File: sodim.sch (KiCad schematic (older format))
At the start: 1 part, among them J1 ddr4-sodimm-edge-connector

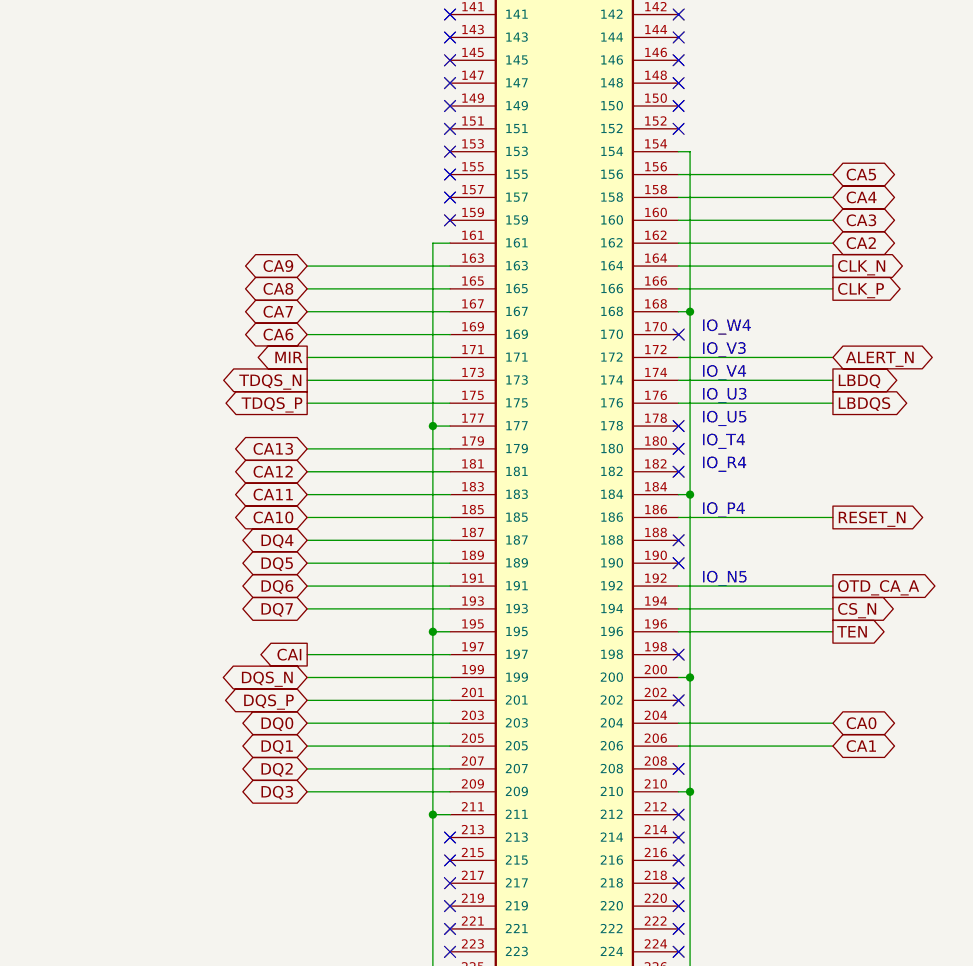
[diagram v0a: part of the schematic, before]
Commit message: Update pin assignment
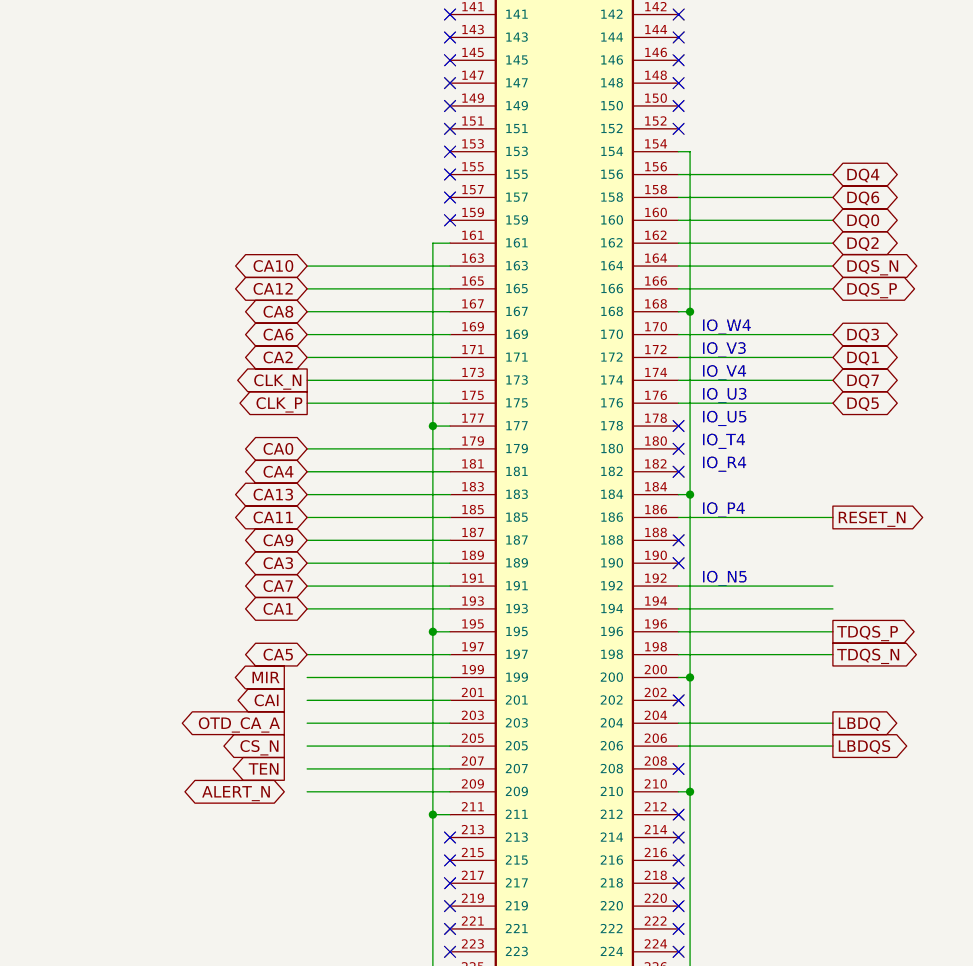
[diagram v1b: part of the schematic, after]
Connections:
- wire segments 183 -> 185
- no-connect marks 149 -> 147
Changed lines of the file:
@@
 Connection ~ 10550 5200
 Wire Wire Line
-	10550 5200 10550 6000
-Wire Wire Line
 	10500 5600 11175 5600
 Wire Wire Line
@@
 Wire Wire Line
 	4075 8900 4725 8900
-Text GLabel 8875 5400 0    50   BiDi ~ 0
+Text GLabel 11175 3800 2    50   BiDi ~ 0
 DQ4
-Text GLabel 8875 5500 0    50   BiDi ~ 0
+Text GLabel 11175 4800 2    50   BiDi ~ 0
 DQ5
-Text GLabel 8875 5600 0    50   BiDi ~ 0
+Text GLabel 11175 3900 2    50   BiDi ~ 0
 DQ6
-Text GLabel 8875 5700 0    50   BiDi ~ 0
+Text GLabel 11175 4700 2    50   BiDi ~ 0
 DQ7
-Text GLabel 8875 6500 0    50   BiDi ~ 0
+Text GLabel 11175 4500 2    50   BiDi ~ 0
 DQ3
-Text GLabel 8875 6400 0    50   BiDi ~ 0
+Text GLabel 11175 4100 2    50   BiDi ~ 0
 DQ2
-Text GLabel 8875 6300 0    50   BiDi ~ 0
+Text GLabel 11175 4600 2    50   BiDi ~ 0
 DQ1
-Text GLabel 8875 6200 0    50   BiDi ~ 0
+Text GLabel 11175 4000 2    50   BiDi ~ 0
 DQ0
-Text GLabel 11175 4300 2    50   Output ~ 0
-CLK_P
-Text GLabel 11175 4200 2    50   Output ~ 0
-CLK_N
-Text GLabel 11175 6200 2    50   BiDi ~ 0
-CA0
-Text GLabel 11175 5700 2    50   Output ~ 0
-CS_N
 Text GLabel 11175 5300 2    50   Output ~ 0
 RESET_N
-Text GLabel 11175 5600 2    50   Output ~ 0
+Text GLabel 8775 6200 0    50   Output ~ 0
 OTD_CA_A
-Text GLabel 8875 4800 0    50   Output ~ 0
-TDQS_P
-Text GLabel 8875 4700 0    50   Output ~ 0
-TDQS_N
-Text GLabel 8875 6100 0    50   BiDi ~ 0
-DQS_P
-Text GLabel 8875 6000 0    50   BiDi ~ 0
-DQS_N
-Text GLabel 11175 6300 2    50   BiDi ~ 0
-CA1
-Text GLabel 11175 4100 2    50   BiDi ~ 0
-CA2
-Text GLabel 11175 4000 2    50   BiDi ~ 0
-CA3
-Text GLabel 11175 3900 2    50   BiDi ~ 0
-CA4
-Text GLabel 11175 3800 2    50   BiDi ~ 0
-CA5
-Text GLabel 8875 4500 0    50   BiDi ~ 0
-CA6
-Text GLabel 8875 4400 0    50   BiDi ~ 0
-CA7
-Text GLabel 8875 4300 0    50   BiDi ~ 0
-CA8
-Text GLabel 8875 4200 0    50   BiDi ~ 0
-CA9
-Text GLabel 8875 5300 0    50   BiDi ~ 0
-CA10
-Text GLabel 8875 5200 0    50   BiDi ~ 0
-CA11
-Text GLabel 8875 5100 0    50   BiDi ~ 0
-CA12
-Text GLabel 8875 5000 0    50   BiDi ~ 0
-CA13
-Text GLabel 11175 4700 2    50   Output ~ 0
+Text GLabel 11175 6200 2    50   Output ~ 0
 LBDQ
-Text GLabel 11175 4800 2    50   Output ~ 0
+Text GLabel 11175 6300 2    50   Output ~ 0
 LBDQS
-Text GLabel 11175 5800 2    50   Output ~ 0
+Text GLabel 8775 6400 0    50   Output ~ 0
 TEN
-Text GLabel 8875 4600 0    50   Output ~ 0
-MIR
-Text GLabel 8875 5900 0    50   Output ~ 0
+Text GLabel 8775 6100 0    50   Output ~ 0
 CAI
 Wire Wire Line
 	10500 4600 11175 4600
-Text GLabel 11175 4600 2    50   BiDi ~ 0
+Text GLabel 8775 6500 0    50   BiDi ~ 0
 ALERT_N
-NoConn ~ 10500 4500
 NoConn ~ 10500 4900
 NoConn ~ 10500 5000
@@
 NoConn ~ 10500 7100
 NoConn ~ 10500 6400
-NoConn ~ 10500 5900
 NoConn ~ 9500 3700
 NoConn ~ 9500 3800
@@
 NoConn ~ 10500 8400
 NoConn ~ 10500 8500
+Text GLabel 8775 6300 0    50   Output ~ 0
+CS_N
+Text GLabel 8875 5200 0    50   BiDi ~ 0
+CA13
+Text GLabel 8875 4300 0    50   BiDi ~ 0
+CA12
+Text GLabel 8875 5300 0    50   BiDi ~ 0
+CA11
+Text GLabel 8875 4200 0    50   BiDi ~ 0
+CA10
+Text GLabel 8875 5700 0    50   BiDi ~ 0
+CA1
+Text GLabel 8875 5000 0    50   BiDi ~ 0
+CA0
+Text GLabel 8875 5400 0    50   BiDi ~ 0
+CA9
+Text GLabel 8875 4400 0    50   BiDi ~ 0
+CA8
+Text GLabel 8875 5600 0    50   BiDi ~ 0
+CA7
+Text GLabel 8875 4500 0    50   BiDi ~ 0
+CA6
+Text GLabel 8775 6000 0    50   Output ~ 0
+MIR
+Text GLabel 8875 5900 0    50   BiDi ~ 0
+CA5
+Text GLabel 8875 5100 0    50   BiDi ~ 0
+CA4
+Text GLabel 8875 5500 0    50   BiDi ~ 0
+CA3
+Text GLabel 8875 4600 0    50   BiDi ~ 0
+CA2
+Text GLabel 11175 4200 2    50   BiDi ~ 0
+DQS_N
+Text GLabel 11175 4300 2    50   BiDi ~ 0
+DQS_P
+Text GLabel 8875 4700 0    50   Output ~ 0
+CLK_N
+Text GLabel 8875 4800 0    50   Output ~ 0
+CLK_P
+Text GLabel 11175 5900 2    50   Output ~ 0
+TDQS_N
+Text GLabel 11175 5800 2    50   Output ~ 0
+TDQS_P
+Wire Wire Line
+	10550 5200 10550 6000
+Wire Wire Line
+	10500 5900 11175 5900
+Wire Wire Line
+	10500 4500 11175 4500
 $EndSCHEMATC

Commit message: Update signal assignment
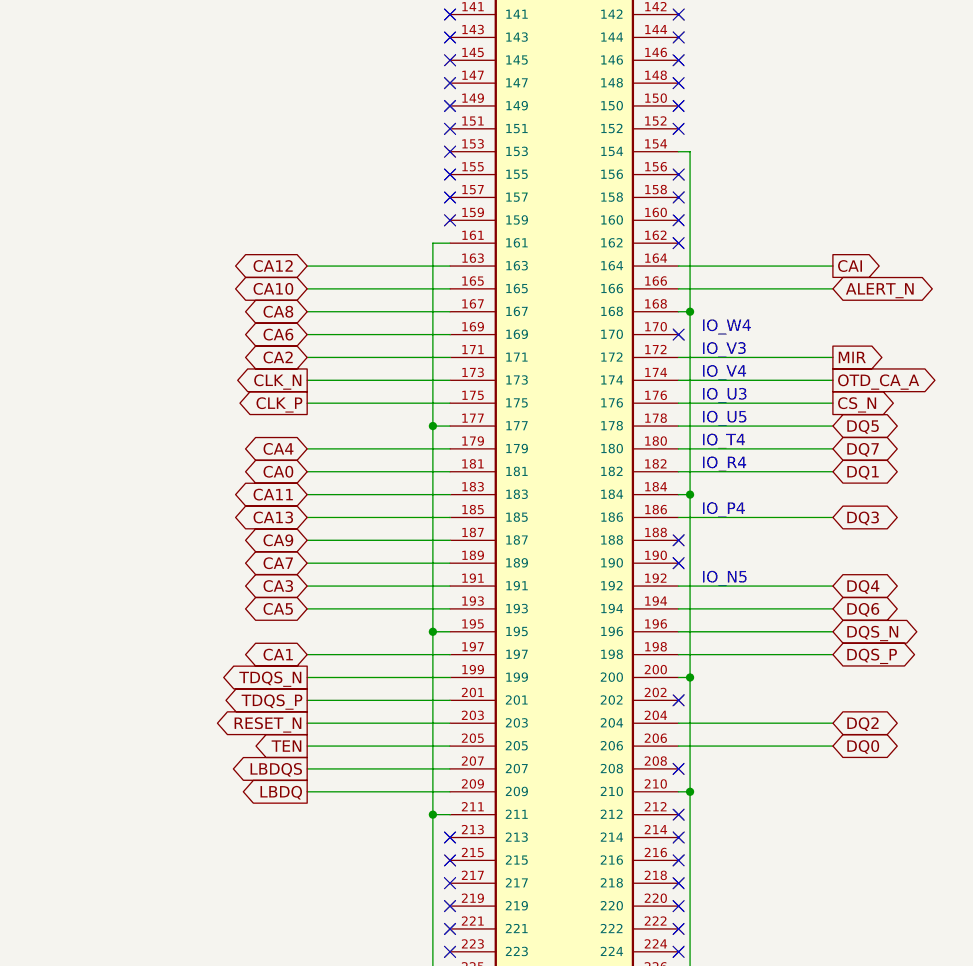
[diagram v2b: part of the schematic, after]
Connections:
- wire segments 185 -> 183
- no-connect marks 147 -> 149
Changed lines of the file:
@@
 $EndComp
 Wire Wire Line
-	10500 3800 11175 3800
-Wire Wire Line
-	10500 3900 11175 3900
-Wire Wire Line
-	10500 4000 11175 4000
-Wire Wire Line
-	10500 4100 11175 4100
-Wire Wire Line
 	10500 4200 11175 4200
 Wire Wire Line
@@
 Wire Wire Line
 	4075 8900 4725 8900
-Text GLabel 11175 3800 2    50   BiDi ~ 0
+Text GLabel 11175 5600 2    50   BiDi ~ 0
 DQ4
-Text GLabel 11175 4800 2    50   BiDi ~ 0
+Text GLabel 11175 4900 2    50   BiDi ~ 0
 DQ5
-Text GLabel 11175 3900 2    50   BiDi ~ 0
+Text GLabel 11175 5700 2    50   BiDi ~ 0
 DQ6
-Text GLabel 11175 4700 2    50   BiDi ~ 0
+Text GLabel 11175 5000 2    50   BiDi ~ 0
 DQ7
-Text GLabel 11175 4500 2    50   BiDi ~ 0
+Text GLabel 11175 5300 2    50   BiDi ~ 0
 DQ3
-Text GLabel 11175 4100 2    50   BiDi ~ 0
+Text GLabel 11175 6200 2    50   BiDi ~ 0
 DQ2
-Text GLabel 11175 4600 2    50   BiDi ~ 0
+Text GLabel 11175 5100 2    50   BiDi ~ 0
 DQ1
-Text GLabel 11175 4000 2    50   BiDi ~ 0
+Text GLabel 11175 6300 2    50   BiDi ~ 0
 DQ0
-Text GLabel 11175 5300 2    50   Output ~ 0
+Text GLabel 8875 6200 0    50   Output ~ 0
 RESET_N
-Text GLabel 8775 6200 0    50   Output ~ 0
+Text GLabel 11175 4700 2    50   Output ~ 0
 OTD_CA_A
-Text GLabel 11175 6200 2    50   Output ~ 0
+Text GLabel 8875 6500 0    50   Output ~ 0
 LBDQ
-Text GLabel 11175 6300 2    50   Output ~ 0
+Text GLabel 8875 6400 0    50   Output ~ 0
 LBDQS
-Text GLabel 8775 6400 0    50   Output ~ 0
+Text GLabel 8875 6300 0    50   Output ~ 0
 TEN
-Text GLabel 8775 6100 0    50   Output ~ 0
+Text GLabel 11175 4200 2    50   Output ~ 0
 CAI
 Wire Wire Line
 	10500 4600 11175 4600
-Text GLabel 8775 6500 0    50   BiDi ~ 0
+Text GLabel 11175 4300 2    50   BiDi ~ 0
 ALERT_N
-NoConn ~ 10500 4900
-NoConn ~ 10500 5000
-NoConn ~ 10500 5100
 Wire Wire Line
 	10500 4700 11175 4700
@@
 NoConn ~ 10500 8400
 NoConn ~ 10500 8500
-Text GLabel 8775 6300 0    50   Output ~ 0
+Text GLabel 11175 4800 2    50   Output ~ 0
 CS_N
-Text GLabel 8875 5200 0    50   BiDi ~ 0
+Text GLabel 8875 5300 0    50   BiDi ~ 0
 CA13
-Text GLabel 8875 4300 0    50   BiDi ~ 0
+Text GLabel 8875 4200 0    50   BiDi ~ 0
 CA12
-Text GLabel 8875 5300 0    50   BiDi ~ 0
+Text GLabel 8875 5200 0    50   BiDi ~ 0
 CA11
-Text GLabel 8875 4200 0    50   BiDi ~ 0
+Text GLabel 8875 4300 0    50   BiDi ~ 0
 CA10
-Text GLabel 8875 5700 0    50   BiDi ~ 0
+Text GLabel 8875 5900 0    50   BiDi ~ 0
 CA1
-Text GLabel 8875 5000 0    50   BiDi ~ 0
+Text GLabel 8875 5100 0    50   BiDi ~ 0
 CA0
 Text GLabel 8875 5400 0    50   BiDi ~ 0
@@
 Text GLabel 8875 4400 0    50   BiDi ~ 0
 CA8
-Text GLabel 8875 5600 0    50   BiDi ~ 0
+Text GLabel 8875 5500 0    50   BiDi ~ 0
 CA7
 Text GLabel 8875 4500 0    50   BiDi ~ 0
 CA6
-Text GLabel 8775 6000 0    50   Output ~ 0
+Text GLabel 11175 4600 2    50   Output ~ 0
 MIR
-Text GLabel 8875 5900 0    50   BiDi ~ 0
+Text GLabel 8875 5700 0    50   BiDi ~ 0
 CA5
-Text GLabel 8875 5100 0    50   BiDi ~ 0
+Text GLabel 8875 5000 0    50   BiDi ~ 0
 CA4
-Text GLabel 8875 5500 0    50   BiDi ~ 0
+Text GLabel 8875 5600 0    50   BiDi ~ 0
 CA3
 Text GLabel 8875 4600 0    50   BiDi ~ 0
 CA2
-Text GLabel 11175 4200 2    50   BiDi ~ 0
+Text GLabel 11175 5800 2    50   BiDi ~ 0
 DQS_N
-Text GLabel 11175 4300 2    50   BiDi ~ 0
+Text GLabel 11175 5900 2    50   BiDi ~ 0
 DQS_P
 Text GLabel 8875 4700 0    50   Output ~ 0
@@
 Text GLabel 8875 4800 0    50   Output ~ 0
 CLK_P
-Text GLabel 11175 5900 2    50   Output ~ 0
+Text GLabel 8875 6000 0    50   Output ~ 0
 TDQS_N
-Text GLabel 11175 5800 2    50   Output ~ 0
+Text GLabel 8875 6100 0    50   Output ~ 0
 TDQS_P
 Wire Wire Line
@@
 	10500 5900 11175 5900
 Wire Wire Line
-	10500 4500 11175 4500
+	10500 5100 11175 5100
+Wire Wire Line
+	10500 5000 11175 5000
+Wire Wire Line
+	10500 4900 11175 4900
+NoConn ~ 10500 3800
+NoConn ~ 10500 3900
+NoConn ~ 10500 4000
+NoConn ~ 10500 4100
+NoConn ~ 10500 4500
 $EndSCHEMATC
